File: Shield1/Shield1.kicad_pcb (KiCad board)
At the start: 4 copper layers, 12 x 14.2 mm, 26 parts, among them J1 Conn_01x01_Male, J10 Conn_01x01_Male, J11 Conn_01x01_Male, J12 Conn_01x01_Male, J13 Conn_01x01_Male, J14 Conn_01x01_Male, J15 Conn_01x01_Male, J17 Conn_01x01_Male, J2 Conn_01x01_Male, J25 Conn_01x01_Male, J26 Conn_01x01_Male, J27 Conn_01x01_Male, J28 Conn_01x01_Male, J29 Conn_01x01_Male, J3 Conn_01x01_Male, J5 Conn_01x01_Male, J6 Conn_01x01_Male, J7 Conn_01x01_Male, J8 Conn_01x01_Male, J9 Conn_01x01_Male, X1 USB_C_24pins

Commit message: v0.95 need 4 checkup
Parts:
- ?: moved to B.Cu
- moved ? 0.22 mm to (104.8, 23.8)
- moved ? 0.20 mm to (95.2, 23.8)
- moved ? 0.10 mm to (95.7, 26.9)
- turned ? to 180 degrees
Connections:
- ? pad 1: GND1 -> GND3
- ? pad 1: GND2 -> GND
- X1 pad 0: (no net) -> Earth
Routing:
- net GND: track 0.00 -> 6.72 mm
- net Earth: track 0.00 -> 4.80 mm
- net GND1: track 6.29 -> 9.24 mm, vias 0 -> 4
- net GND2: track 12.6 -> 9.89 mm, vias 0 -> 3
- net D-: track 8.57 -> 9.74 mm
- added copper zone on In1.Cu, net GND1
- added copper zone on In2.Cu, net GND1
- added copper zone on B.Cu, net GND2
- added copper zone on In1.Cu, net GND2
- added copper zone on In2.Cu, net GND2
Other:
- board size 12 x 14.2 mm -> 12 x 19 mm
- board text added: "D+"
- board text added: "D-"
- board text added: "PGND"
- board text added: "RX"
- board text added: "TX"
- board text added: "V1"
- board text added: "V2"

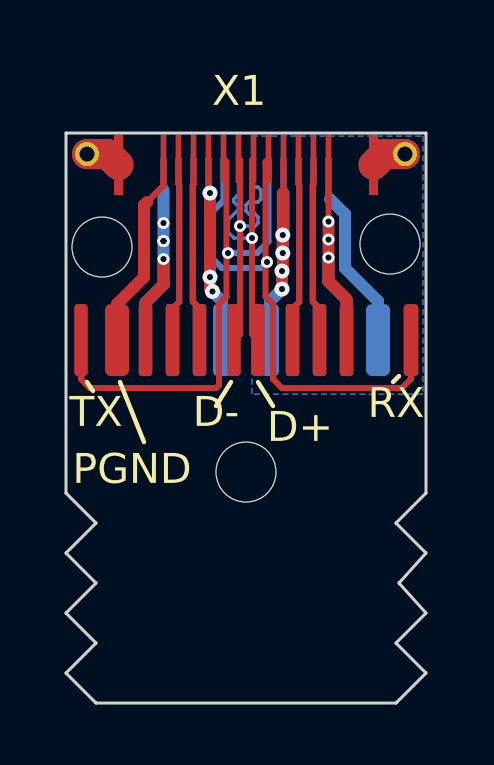
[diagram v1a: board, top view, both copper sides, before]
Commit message: v0.96 Rx, Tx were hidden and moved
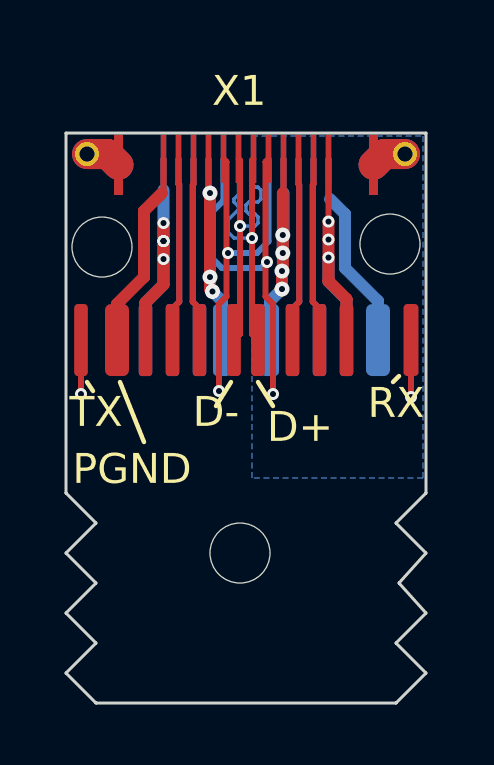
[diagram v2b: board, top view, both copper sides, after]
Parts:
- moved ? 2.71 mm to (99.8, 34.0)
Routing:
- net RX: track 19.1 -> 24.5 mm, vias 1 -> 3
- net TX: track 18.0 -> 23.2 mm, vias 1 -> 3
- net GND1: track 9.24 -> 10.4 mm
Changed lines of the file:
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@@
   )
   (footprint "" (layer "F.Cu")
-    (at 100 31.3)
+    (at 99.8 34)
     (fp_text reference "" (at 0 0) (layer "F.SilkS")
       (effects (font (size 1.27 1.27) (thickness 0.15)))
@@
   (segment (start 97.25 24.2) (end 97.25 25.05) (width 0.4) (layer "F.Cu") (net 1))
   (segment (start 97.25 25.05) (end 96.65 25.65) (width 0.4) (layer "F.Cu") (net 1))
+  (segment (start 97.25 24.2) (end 97.25 23) (width 0.4) (layer "F.Cu") (net 1))
   (via (at 97.25 24.2) (size 0.4) (drill 0.2) (layers "F.Cu" "B.Cu") (net 1))
   (via (at 97.25 23.6) (size 0.4) (drill 0.2) (layers "F.Cu" "B.Cu") (net 1))
@@
   (segment (start 99.6 22.2) (end 99.6 22.3) (width 0.112) (layer "B.Cu") (net 7))
   (segment (start 99.75 22.05) (end 99.6 22.2) (width 0.112) (layer "B.Cu") (net 7))
+  (segment (start 105.5 28.8) (end 105.5 26.9) (width 0.2) (layer "F.Cu") (net 8))
+  (segment (start 100.75 20.86) (end 100.650489 20.959511) (width 0.2) (layer "F.Cu") (net 8))
+  (segment (start 100.9 25.7) (end 100.9 28.7) (width 0.2) (layer "F.Cu") (net 8))
   (segment (start 100.650489 25.450489) (end 100.9 25.7) (width 0.2) (layer "F.Cu") (net 8))
-  (segment (start 100.75 20.86) (end 100.650489 20.959511) (width 0.2) (layer "F.Cu") (net 8))
-  (segment (start 100.9 25.7) (end 100.9 28.2) (width 0.2) (layer "F.Cu") (net 8))
-  (segment (start 105.5 28.2) (end 105.5 26.9) (width 0.2) (layer "F.Cu") (net 8))
-  (segment (start 101.2 28.5) (end 105.2 28.5) (width 0.2) (layer "F.Cu") (net 8))
   (segment (start 100.650489 20.959511) (end 100.650489 25.450489) (width 0.2) (layer "F.Cu") (net 8))
-  (segment (start 105.2 28.5) (end 105.5 28.2) (width 0.2) (layer "F.Cu") (net 8))
-  (segment (start 100.9 28.2) (end 101.2 28.5) (width 0.2) (layer "F.Cu") (net 8))
+  (via (at 105.5 28.8) (size 0.4) (drill 0.2) (layers "F.Cu" "B.Cu") (net 8))
   (via (at 100.7 24.3) (size 0.4) (drill 0.2) (layers "F.Cu" "B.Cu") (free) (net 8))
+  (via (at 100.9 28.7) (size 0.4) (drill 0.2) (layers "F.Cu" "B.Cu") (net 8))
+  (segment (start 100.9 30.9) (end 100.9 28.7) (width 0.2) (layer "In2.Cu") (net 8))
+  (segment (start 105.2 31.2) (end 101.2 31.2) (width 0.2) (layer "In2.Cu") (net 8))
+  (segment (start 105.5 30.9) (end 105.2 31.2) (width 0.2) (layer "In2.Cu") (net 8))
+  (segment (start 105.5 28.8) (end 105.5 30.9) (width 0.2) (layer "In2.Cu") (net 8))
+  (segment (start 101.2 31.2) (end 100.9 30.9) (width 0.2) (layer "In2.Cu") (net 8))
   (segment (start 99.2 24.5) (end 100.5 24.5) (width 0.2) (layer "B.Cu") (net 8))
   (segment (start 99.25 22.25) (end 98.9 22.6) (width 0.2) (layer "B.Cu") (net 8))
@@
   (segment (start 102.45 25.85) (end 102.45 26.9) (width 0.2) (layer "F.Cu") (net 16))
   (segment (start 102.25 21.7) (end 102.225001 21.724999) (width 0.2) (layer "F.Cu") (net 16))
-  (segment (start 94.8 28.5) (end 94.5 28.2) (width 0.2) (layer "F.Cu") (net 17))
-  (segment (start 99 28.5) (end 94.8 28.5) (width 0.2) (layer "F.Cu") (net 17))
+  (segment (start 94.5 28.7) (end 94.5 26.9) (width 0.2) (layer "F.Cu") (net 17))
+  (segment (start 99.1 25.7) (end 99.1 28.6) (width 0.2) (layer "F.Cu") (net 17))
+  (segment (start 99.349511 25.450489) (end 99.1 25.7) (width 0.2) (layer "F.Cu") (net 17))
+  (segment (start 99.349511 20.959511) (end 99.349511 25.450489) (width 0.2) (layer "F.Cu") (net 17))
   (segment (start 99.25 20.86) (end 99.349511 20.959511) (width 0.2) (layer "F.Cu") (net 17))
-  (segment (start 94.5 28.2) (end 94.5 26.9) (width 0.2) (layer "F.Cu") (net 17))
-  (segment (start 99.349511 20.959511) (end 99.349511 25.450489) (width 0.2) (layer "F.Cu") (net 17))
-  (segment (start 99.349511 25.450489) (end 99.1 25.7) (width 0.2) (layer "F.Cu") (net 17))
-  (segment (start 99.1 25.7) (end 99.1 28.4) (width 0.2) (layer "F.Cu") (net 17))
-  (segment (start 99.1 28.4) (end 99 28.5) (width 0.2) (layer "F.Cu") (net 17))
+  (via (at 94.5 28.7) (size 0.4) (drill 0.2) (layers "F.Cu" "B.Cu") (net 17))
   (via (at 99.4 24) (size 0.4) (drill 0.2) (layers "F.Cu" "B.Cu") (free) (net 17))
+  (via (at 99.1 28.6) (size 0.4) (drill 0.2) (layers "F.Cu" "B.Cu") (net 17))
+  (segment (start 99.1 30.9) (end 98.9 31.1) (width 0.2) (layer "In2.Cu") (net 17))
+  (segment (start 98.9 31.1) (end 94.8 31.1) (width 0.2) (layer "In2.Cu") (net 17))
+  (segment (start 99.1 28.6) (end 99.1 30.9) (width 0.2) (layer "In2.Cu") (net 17))
+  (segment (start 94.5 30.8) (end 94.5 28.7) (width 0.2) (layer "In2.Cu") (net 17))
+  (segment (start 94.8 31.1) (end 94.5 30.8) (width 0.2) (layer "In2.Cu") (net 17))
   (segment (start 100.75 23.612183) (end 100.75 20.86) (width 0.2) (layer "B.Cu") (net 17))
   (segment (start 100.362183 24) (end 100.75 23.612183) (width 0.2) (layer "B.Cu") (net 17))
@@
   (segment (start 103.3 24.5) (end 104.4 25.6) (width 0.4) (layer "B.Cu") (net 18))
   (segment (start 103.3 22.7) (end 103.3 24.5) (width 0.4) (layer "B.Cu") (net 18))
+  (segment (start 97.2 22) (end 97.25 21.95) (width 0.2) (layer "F.Cu") (net 19))
+  (segment (start 96.599521 22.600479) (end 96.599521 24.800479) (width 0.4) (layer "F.Cu") (net 19))
+  (segment (start 97.2 22) (end 96.599521 22.600479) (width 0.4) (layer "F.Cu") (net 19))
   (segment (start 95.7 25.7) (end 95.7 26.9) (width 0.4) (layer "F.Cu") (net 19))
-  (segment (start 97 22) (end 96.7 22.3) (width 0.2) (layer "F.Cu") (net 19))
-  (segment (start 96.7 22.3) (end 96.599521 22.400479) (width 0.4) (layer "F.Cu") (net 19))
-  (segment (start 97.25 21.75) (end 97 22) (width 0.2) (layer "F.Cu") (net 19))
+  (segment (start 97.25 21.95) (end 97.25 20.86) (width 0.2) (layer "F.Cu") (net 19))
   (segment (start 96.599521 24.800479) (end 95.7 25.7) (width 0.4) (layer "F.Cu") (net 19))
-  (segment (start 97.25 20.86) (end 97.25 21.75) (width 0.2) (layer "F.Cu") (net 19))
-  (segment (start 96.599521 22.400479) (end 96.599521 24.800479) (width 0.4) (layer "F.Cu") (net 19))
   (zone (net 1) (net_name "GND1") (layers "In1.Cu" "In2.Cu") (hatch edge 0.508)
     (connect_pads (clearance 0.2))
@@
     (polygon
       (pts
-        (xy 99.8 28.7)
-        (xy 94.1 28.6)
+        (xy 99.750892 31.499133)
+        (xy 94.050892 31.399133)
         (xy 94.1 20.1)
         (xy 99.8 20.1)
@@
     (polygon
       (pts
-        (xy 105.9 28.7)
-        (xy 100.2 28.7)
+        (xy 105.9 31.5)
+        (xy 100.2 31.5)
         (xy 100.2 20.1)
         (xy 105.9 20.1)

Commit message: v0.97 Seems 2B ready
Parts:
- moved ? 0.20 mm to (100.0, 34.0)
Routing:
- net TX: track 23.2 -> 26.2 mm
- net RX: track 24.5 -> 27.5 mm
- net GND2: track 9.89 -> 10.6 mm
- removed copper zone on B.Cu, net GND2
